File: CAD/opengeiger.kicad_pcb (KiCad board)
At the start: 2 copper layers, 123.8 x 66.8 mm, 77 parts, among them J1 Conn_01x02, J10 Conn_01x04, J2 Conn_01x02, J3 Conn_01x06, J5 Conn_01x04, J7 Conn_01x02, J8 USB_C_Receptacle_USB2.0, Q1 STN0214, Q2 PMBT2222A,215, Q3 DMG2302UK-7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

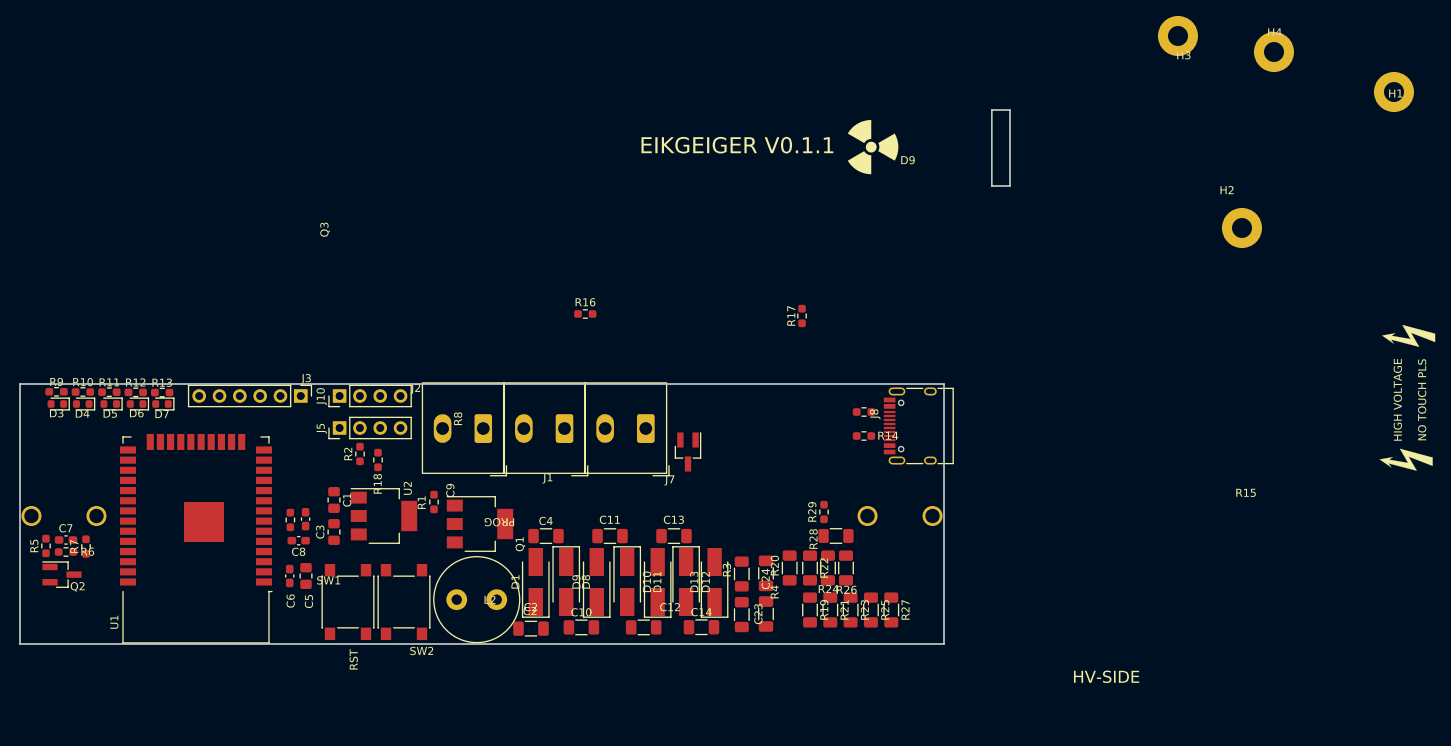
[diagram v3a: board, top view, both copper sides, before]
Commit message: Feat: Slimmify more and usb uart
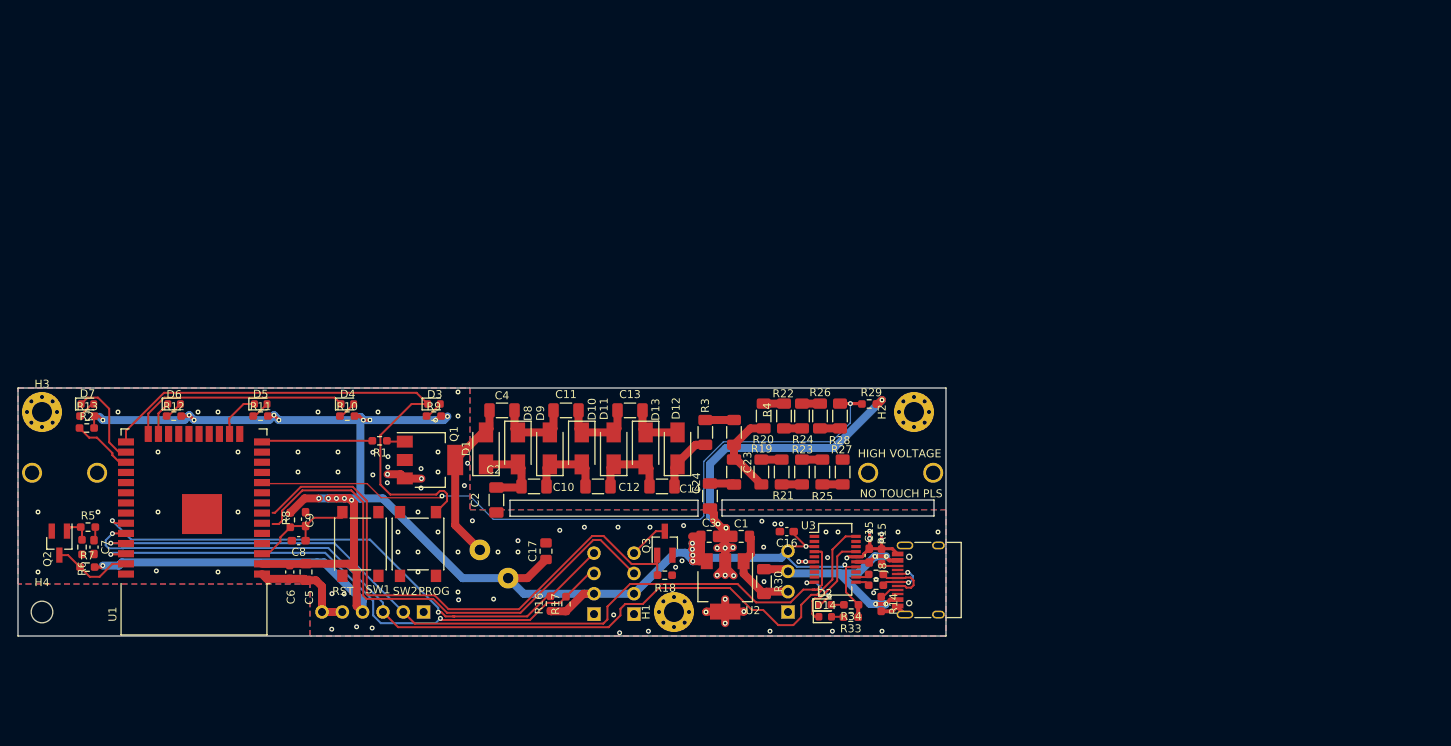
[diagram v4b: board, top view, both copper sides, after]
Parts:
- removed J2, J7: Conn_01x02, Fredriklib:TB010-508-02BE
- added C15: 0.1uF, Capacitor_SMD:C_0603_1608Metric_Pad1.08x0.95mm_HandSolder, F.Cu at (171.4, 98.0)
- added C16: 0.1uF, Capacitor_SMD:C_0603_1608Metric_Pad1.08x0.95mm_HandSolder, F.Cu at (161.1, 95.0)
- added C17: 22uF, Capacitor_SMD:C_0805_2012Metric_Pad1.18x1.45mm_HandSolder, F.Cu at (131.0, 97.4)
- added D14: 0603RBD0700S01, LED_SMD:LED_0603_1608Metric, F.Cu at (165.9, 105.6)
- added D2: 0603RBD0700S01, LED_SMD:LED_0603_1608Metric, F.Cu at (165.8, 104.1)
- added R30: 0R, Resistor_SMD:R_1206_3216Metric_Pad1.30x1.75mm_HandSolder, F.Cu at (158.2, 101.2)
- added R31: 47R, Resistor_SMD:R_0603_1608Metric_Pad0.98x0.95mm_HandSolder, F.Cu at (172.2, 100.3)
- added R32: 47R, Resistor_SMD:R_0603_1608Metric_Pad0.98x0.95mm_HandSolder, F.Cu at (172.2, 101.7)
- added R33: 270R, Resistor_SMD:R_0603_1608Metric_Pad0.98x0.95mm_HandSolder, F.Cu at (169.1, 105.7)
- added R34: 270R, Resistor_SMD:R_0603_1608Metric_Pad0.98x0.95mm_HandSolder, F.Cu at (169.2, 104.1)
- added U3: FT231XS, Package_SO:SSOP-20_3.9x8.7mm_P0.635mm, F.Cu at (167.1, 98.4)
- D1, D10, D11, D12, D13, D8, D9: footprint Diode_SMD:D_SMA_Handsoldering -> Diode_SMD:D_SMA
- H1, H2, H3: footprint MountingHole:MountingHole_2.5mm_Pad -> MountingHole:MountingHole_2.5mm_Pad_Via
- H4: footprint MountingHole:MountingHole_2.5mm_Pad -> MountingHole:MountingHole_2.7mm
- J1: value Conn_01x02 -> Conn_01x04; footprint Fredriklib:TB010-508-02BE -> Connector_PinHeader_2.54mm:PinHeader_1x04_P2.54mm_Vertical; moved to B.Cu
- J10, J3, J5, L2: moved to B.Cu
- moved H4 169.2 mm to (68.0, 105.0)
- moved H3 149.6 mm to (68.0, 80.0)
- moved H1 111.0 mm to (147.0, 105.0)
- moved C1 51.1 mm to (155.4, 95.5), turned to 180 degrees
- moved R9 47.3 mm to (117.0, 80.5)
- moved D3 47.1 mm to (117.0, 79.0), turned to 0 degrees
- moved H2 47.0 mm to (177.0, 80.0)
- moved C3 46.9 mm to (151.4, 95.5), turned to 0 degrees
- moved R17 46.5 mm to (133.5, 104.0)
- moved J10 45.8 mm to (142.0, 105.3), turned to 0 degrees
- moved U2 43.5 mm to (153.4, 101.8), turned to -90 degrees
- moved J5 39.4 mm to (137.0, 105.3), turned to 0 degrees
- moved R18 38.6 mm to (145.8, 100.4), turned to 180 degrees
- moved R16 36.5 mm to (131.6, 104.0), turned to 90 degrees
- moved J1 36.1 mm to (161.2, 105.0), turned to 0 degrees
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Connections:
- H1 pad 1: unconnected-(H1-Pad1) -> GNDREF
- H2 pad 1: GNDREF -> unconnected-(H2-Pad1)
- J1 pad 1: +5V -> GNDREF
- J1 pad 2: GNDREF -> +5V
- J10 pad 4: GPIO35 -> Net-(Q3-Pad3)
- J8 pad A4: +5V -> +5V_USB
- J8 pad A6: unconnected-(J8-PadA6) -> Net-(J8-PadA6)
- J8 pad A7: unconnected-(J8-PadA7) -> Net-(J8-PadA7)
- J8 pad A9: +5V -> +5V_USB
- J8 pad B4: +5V -> +5V_USB
- J8 pad B6: unconnected-(J8-PadB6) -> Net-(J8-PadA6)
- J8 pad B7: unconnected-(J8-PadB7) -> Net-(J8-PadA7)
- J8 pad B9: +5V -> +5V_USB
- Q3 pad 3: Net-(J7-Pad2) -> Net-(Q3-Pad3)
- U1 pad 14: unconnected-(U1-Pad14) -> PWM
- U1 pad 16: CLICKER -> LED2
- U1 pad 23: unconnected-(U1-Pad23) -> LED3
- U1 pad 24: GPIO02 -> LED1
- U1 pad 26: PULSE -> LED4
- U1 pad 28: LED1 -> unconnected-(U1-Pad28)
- U1 pad 29: PWM -> unconnected-(U1-Pad29)
- U1 pad 30: LED2 -> unconnected-(U1-Pad30)
- U1 pad 31: LED3 -> unconnected-(U1-Pad31)
- U1 pad 37: LED4 -> PULSE
- U1 pad 6: GPIO34 -> GPIO32
- U1 pad 7: GPIO35 -> CLICKER
- U1 pad 8: GPIO32 -> unconnected-(U1-Pad8)
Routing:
- net +3.3V: track 0.00 -> 251.1 mm, vias 0 -> 21
- net RXD: track 0.00 -> 114.6 mm, vias 0 -> 1
- net TXD: track 0.00 -> 105.2 mm, vias 0 -> 1
- net GNDREF: track 0.00 -> 97.8 mm, vias 0 -> 97
- net RFB: track 0.00 -> 89.8 mm, vias 0 -> 2
- net SDA: track 0.00 -> 70.8 mm, vias 0 -> 2
- net CLICKER: track 0.00 -> 70.4 mm
- net SCL: track 0.00 -> 70.1 mm, vias 0 -> 2
- net PGM/GPIO0: track 0.00 -> 67.4 mm
- net GPIO32: track 0.00 -> 66.3 mm
- net +5V_USB: track 0.00 -> 33.5 mm, vias 0 -> 4
- net LED1: track 0.00 -> 27.8 mm
- net Net-(C4-Pad1): track 0.00 -> 21.3 mm
- net RST: track 0.00 -> 14.1 mm
- net PWM: track 0.00 -> 13.8 mm
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- added copper zone on B.Cu, net GNDREF
- added copper zone on F.Cu, net GNDREF
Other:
- board size 123.8 x 66.8 mm -> 116 x 31 mm
- board text added: "EIKGEIGER V0.2.0"
- board text removed: "D9"
- board text removed: "EIKGEIGER V0.1.1"
- board text removed: "HV-SIDE"

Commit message: Feat:WIP Rounding tracks
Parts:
- removed G*: SBM-20, eikgeiger:SBM-20
- added FID1: Fiducial, Fiducial:Fiducial_1mm_Mask2mm, F.Cu at (174.4, 78.3)
- added FID2: Fiducial, Fiducial:Fiducial_1mm_Mask2mm, F.Cu at (171.9, 106.5)
- added FID3: Fiducial, Fiducial:Fiducial_1mm_Mask2mm, F.Cu at (79.0, 79.0)
- added G1: GM_tube_HOLDERS, eikgeiger:SBM-20, B.Cu at (123.1, 87.6)
- added Q4: UMH3N, Package_TO_SOT_SMD:SOT-363_SC-70-6, F.Cu at (107.4, 86.2)
- added kibuzzard-637F3F6B: G***, kibuzzard-637F3F6B, B.Cu at (86.5, 95.8)
- H2: footprint MountingHole:MountingHole_2.5mm_Pad_Via -> MountingHole:MountingHole_2.5mm
- moved C1 3.00 mm to (152.4, 95.5)
- moved C15 3.00 mm to (168.4, 98.0)
- moved C16 3.00 mm to (158.1, 95.0)
- moved C3 3.00 mm to (148.4, 95.5)
- moved D14 3.00 mm to (162.9, 105.6)
- moved D2 3.00 mm to (162.8, 104.1)
- moved H1 3.00 mm to (144.0, 105.0)
- moved J1 3.00 mm to (158.2, 105.0)
- moved J10 3.00 mm to (139.0, 105.3)
- moved J5 3.00 mm to (134.0, 105.3)
- moved Q3 3.00 mm to (142.8, 96.4)
- moved R14 3.00 mm to (169.9, 104.0)
- moved R15 3.00 mm to (169.9, 98.0)
- moved R18 3.00 mm to (142.8, 100.4)
- moved R30 3.00 mm to (155.2, 101.2)
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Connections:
- net Net-(C14-Pad2) renamed /HV_A
- net Net-(C23-Pad2) renamed /HV_B
- net Net-(C4-Pad1) renamed /SWITCH
- net Net-(D14-Pad1) renamed /CBUS1
- net Net-(D2-Pad1) renamed /CBUS2
- net Net-(J8-PadA5) renamed /CC1
- net Net-(J8-PadA6) renamed /DP*
- net Net-(J8-PadA7) renamed /DM*
- net Net-(J8-PadB5) renamed /CC2
- net Net-(U3-Pad11) renamed /DP
- net Net-(U3-Pad12) renamed /DM
- R27 pad 1: Net-(J4-Pad2) -> /HV_C
- U3 pad 1: unconnected-(U3-Pad1) -> DTR#
- U3 pad 2: unconnected-(U3-Pad2) -> RTS#
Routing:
- net RTS#: track 0.00 -> 79.4 mm, vias 0 -> 4
- net DTR#: track 0.00 -> 76.5 mm, vias 0 -> 4
- net GNDREF: track 97.8 -> 132.2 mm, vias 97 -> 164
- net +3.3V: track 251.1 -> 273.4 mm, vias 21 -> 23
- net RST: track 14.1 -> 30.1 mm, vias 0 -> 2
- net Net-(C7-Pad1): track 1.70 -> 17.1 mm
- net /HV_C: track 0.00 -> 11.9 mm
- net +5V_USB: track 33.5 -> 42.2 mm, vias 4 -> 6
- net PGM/GPIO0: track 67.4 -> 73.2 mm, vias 0 -> 3
- net RXD: track 114.6 -> 109.8 mm
- net GPIO32: track 66.3 -> 62.6 mm
- net TXD: track 105.2 -> 101.6 mm
- net CLICKER: track 70.4 -> 66.9 mm
- net SCL: track 70.1 -> 66.6 mm
- net SDA: track 70.8 -> 67.6 mm
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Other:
- outline, holes or cut-outs redrawn
- board text added: "V 0.2.0"
- board text removed: "EIKGEIGER V0.2.0"

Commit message: Feat:Round Corners, temp gerber production
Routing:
- net /HV_B: track 8.97 -> 8.40 mm
- net GNDREF: vias 164 -> 170

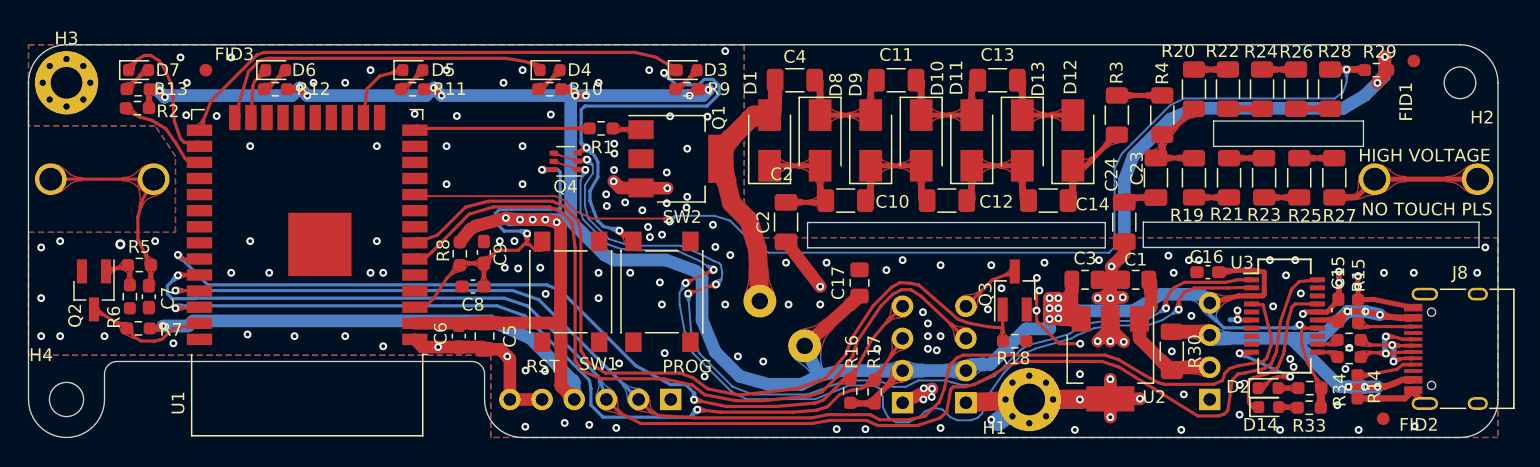
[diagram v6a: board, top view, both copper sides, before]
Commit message: Feat: Production files for JLC prod, readme update
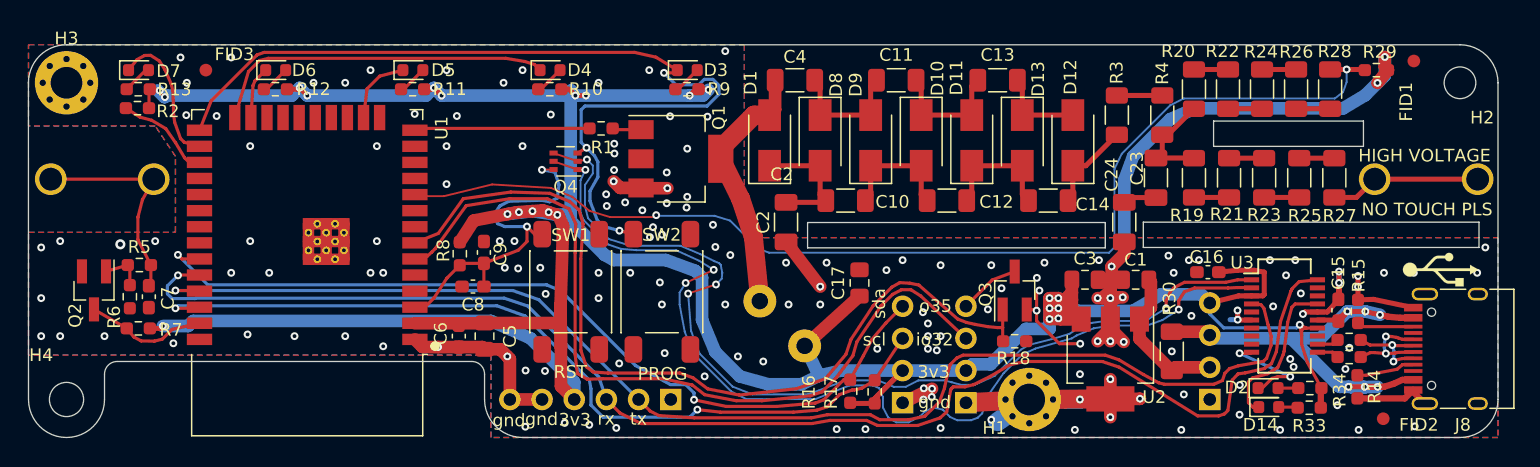
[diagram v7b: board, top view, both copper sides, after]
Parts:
- added G***: LOGO, LOGO, B.Cu at (166.5, 99.5)
- SW1, SW2: footprint Button_Switch_SMD:SW_SPST_PTS645 -> eikgeiger:SW_TL3301NF160QG_TR
- U1: footprint RF_Module:ESP32-WROOM-32 -> eikgeiger:ESP32-WROOM-32
- moved kibuzzard-637F3F6B 0.82 mm to (86.0, 96.5)
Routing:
- net GNDREF: track 132.2 -> 149.0 mm, vias 170 -> 169
- net +3.3V: track 273.3 -> 276.2 mm
- net RST: track 30.4 -> 28.1 mm
- net GPIO32: track 62.6 -> 64.3 mm
- net CLICKER: track 66.9 -> 68.5 mm
- net /SWITCH: track 21.2 -> 20.5 mm
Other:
- board text added: "3v3"
- board text added: "3v3_REG"
- board text added: "5v0_USB"
- board text added: "5v0_card"
- board text added: "GND"
- board text added: "gnd"
- board text added: "io32"
- board text added: "o35"
- board text added: "rx"
- board text added: "scl"
- board text added: "sda"
- board text added: "tx"

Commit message: Feat: New prod, working code
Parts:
- H4: footprint MountingHole:MountingHole_2.7mm -> MountingHole:MountingHole_2.5mm
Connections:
- U1 pad 6: GPIO32 -> unconnected-(U1-Pad6)
- U1 pad 7: CLICKER -> unconnected-(U1-Pad7)
- U1 pad 8: unconnected-(U1-Pad8) -> CLICKER
- U1 pad 9: unconnected-(U1-Pad9) -> GPIO32
- U3 pad 13: unconnected-(U3-Pad13) -> 3v3fdti
- U3 pad 14: +3.3V -> 3v3fdti
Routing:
- net +3.3V: track 276.2 -> 273.2 mm
- net 3v3fdti: track 0.00 -> 1.88 mm
- net GPIO32: track 64.3 -> 63.1 mm, vias 0 -> 2
- net CLICKER: track 68.5 -> 67.7 mm
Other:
- board text added: "V 0.2.1"
- board text removed: "C2"
- board text removed: "V 0.2.0"
